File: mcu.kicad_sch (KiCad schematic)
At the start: 11 parts, among them U5 ESP32-S3-WROOM-1

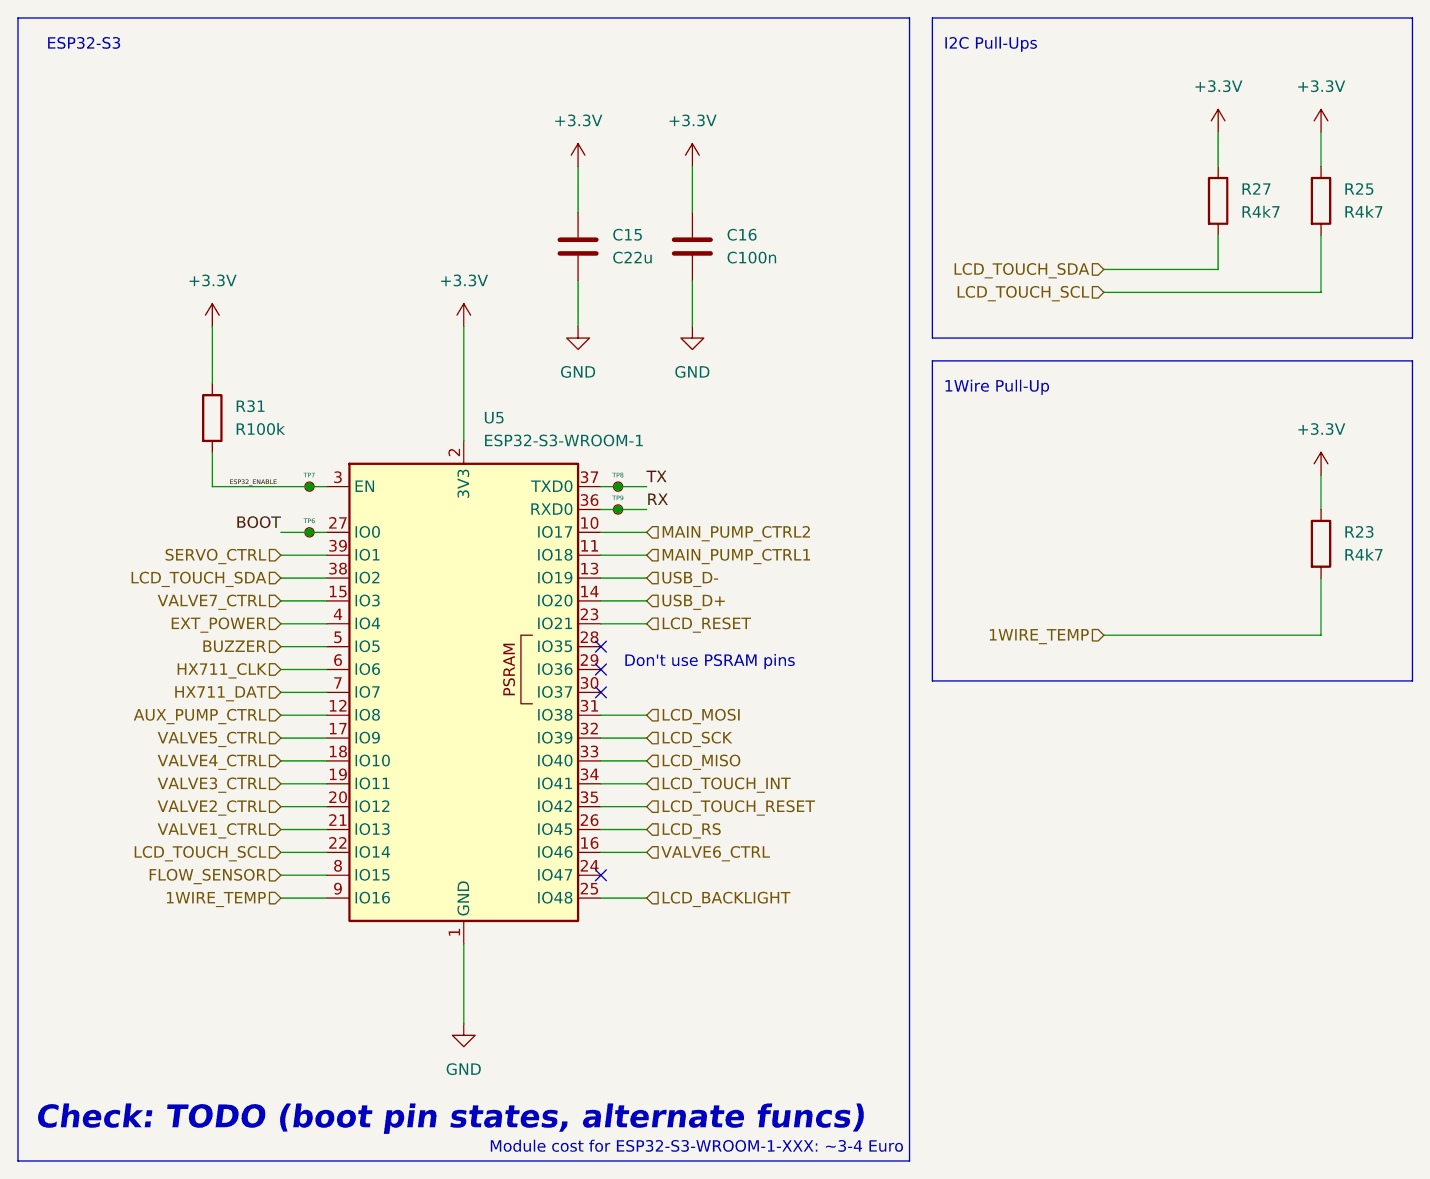
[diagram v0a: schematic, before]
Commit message: Reannotate geographically by layout
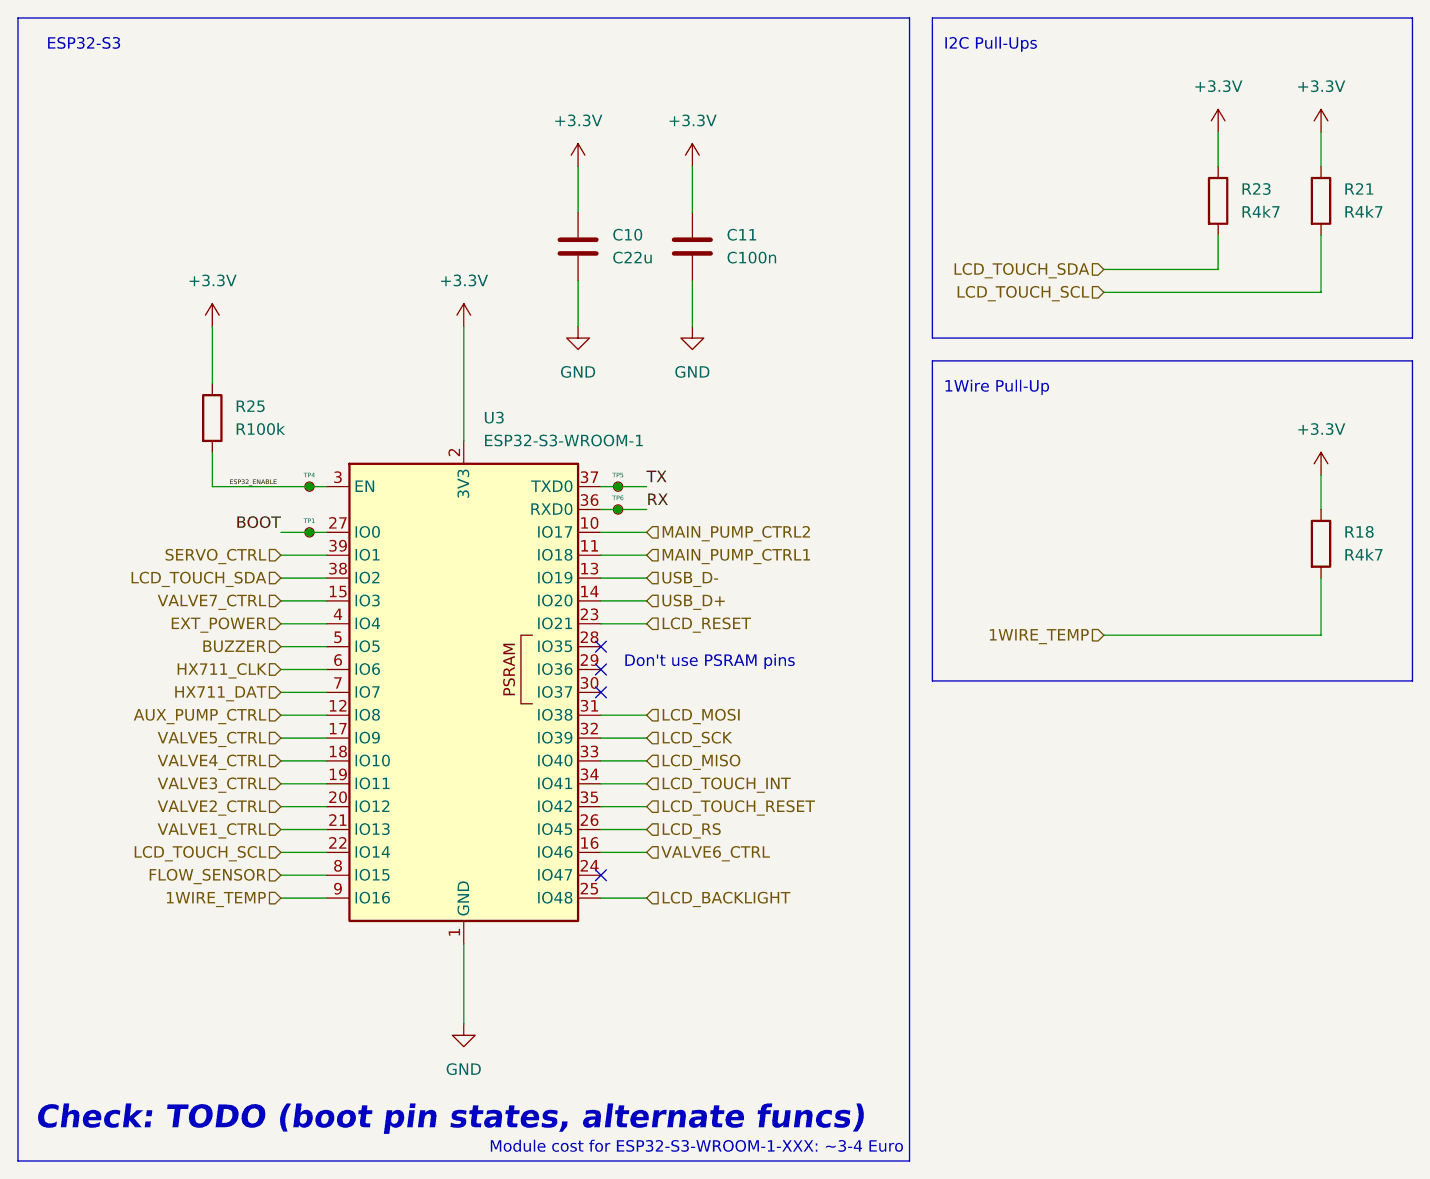
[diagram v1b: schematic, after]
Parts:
- renumbered C15 to C10, C16 to C11, R23 to R18, R25 to R21, R27 to R23, R31 to R25, TP6 to TP1, TP7 to TP4, TP8 to TP5, TP9 to TP6, U5 to U3
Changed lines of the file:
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@@
   (symbol (lib_id "Connector:TestPoint_Small") (at 46.355 82.55 0) (unit 1)
     (in_bom yes) (on_board yes) (dnp no)
-    (property "Reference" "TP7" (at 46.355 81.28 0)
+    (property "Reference" "TP4" (at 46.355 81.28 0)
       (effects (font (size 0.504 0.504)))
     )
@@
       (project "mainboard"
         (path "/613f8c39-c37c-4981-8911-5138d36a7959/ed2e236e-cfd2-4567-8f0f-a7cfa7de4717"
-          (reference "TP7") (unit 1)
+          (reference "TP4") (unit 1)
         )
       )
@@
   (symbol (lib_id "Connector:TestPoint_Small") (at 80.645 82.55 0) (unit 1)
     (in_bom yes) (on_board yes) (dnp no)
-    (property "Reference" "TP8" (at 80.645 81.28 0)
+    (property "Reference" "TP5" (at 80.645 81.28 0)
       (effects (font (size 0.504 0.504)))
     )
@@
       (project "mainboard"
         (path "/613f8c39-c37c-4981-8911-5138d36a7959/ed2e236e-cfd2-4567-8f0f-a7cfa7de4717"
-          (reference "TP8") (unit 1)
+          (reference "TP5") (unit 1)
         )
       )
@@
   (symbol (lib_id "Device:C") (at 76.2 55.88 0) (unit 1)
     (in_bom yes) (on_board yes) (dnp no) (fields_autoplaced)
-    (property "Reference" "C15" (at 80.01 54.61 0)
+    (property "Reference" "C10" (at 80.01 54.61 0)
       (effects (font (size 1.27 1.27)) (justify left))
     )
@@
       (project "mainboard"
         (path "/613f8c39-c37c-4981-8911-5138d36a7959/ed2e236e-cfd2-4567-8f0f-a7cfa7de4717"
-          (reference "C15") (unit 1)
+          (reference "C10") (unit 1)
         )
       )
@@
   (symbol (lib_id "Connector:TestPoint_Small") (at 80.645 85.09 0) (unit 1)
     (in_bom yes) (on_board yes) (dnp no)
-    (property "Reference" "TP9" (at 80.645 83.82 0)
+    (property "Reference" "TP6" (at 80.645 83.82 0)
       (effects (font (size 0.504 0.504)))
     )
@@
       (project "mainboard"
         (path "/613f8c39-c37c-4981-8911-5138d36a7959/ed2e236e-cfd2-4567-8f0f-a7cfa7de4717"
-          (reference "TP9") (unit 1)
+          (reference "TP6") (unit 1)
         )
       )
@@
   (symbol (lib_id "Device:R") (at 158.75 50.8 0) (unit 1)
     (in_bom yes) (on_board yes) (dnp no) (fields_autoplaced)
-    (property "Reference" "R25" (at 161.29 49.53 0)
+    (property "Reference" "R21" (at 161.29 49.53 0)
       (effects (font (size 1.27 1.27)) (justify left))
     )
@@
       (project "mainboard"
         (path "/613f8c39-c37c-4981-8911-5138d36a7959/ed2e236e-cfd2-4567-8f0f-a7cfa7de4717"
-          (reference "R25") (unit 1)
+          (reference "R21") (unit 1)
         )
       )
@@
   (symbol (lib_id "Connector:TestPoint_Small") (at 46.355 87.63 0) (unit 1)
     (in_bom yes) (on_board yes) (dnp no)
-    (property "Reference" "TP6" (at 46.355 86.36 0)
+    (property "Reference" "TP1" (at 46.355 86.36 0)
       (effects (font (size 0.504 0.504)))
     )
@@
       (project "mainboard"
         (path "/613f8c39-c37c-4981-8911-5138d36a7959/ed2e236e-cfd2-4567-8f0f-a7cfa7de4717"
-          (reference "TP6") (unit 1)
+          (reference "TP1") (unit 1)
         )
       )
@@
   (symbol (lib_id "RF_Module:ESP32-S3-WROOM-1") (at 63.5 105.41 0) (unit 1)
     (in_bom yes) (on_board yes) (dnp no) (fields_autoplaced)
-    (property "Reference" "U5" (at 65.6941 74.93 0)
+    (property "Reference" "U3" (at 65.6941 74.93 0)
       (effects (font (size 1.27 1.27)) (justify left))
     )
@@
       (project "mainboard"
         (path "/613f8c39-c37c-4981-8911-5138d36a7959/ed2e236e-cfd2-4567-8f0f-a7cfa7de4717"
-          (reference "U5") (unit 1)
+          (reference "U3") (unit 1)
         )
       )
@@
   (symbol (lib_id "Device:R") (at 147.32 50.8 0) (unit 1)
     (in_bom yes) (on_board yes) (dnp no) (fields_autoplaced)
-    (property "Reference" "R27" (at 149.86 49.53 0)
+    (property "Reference" "R23" (at 149.86 49.53 0)
       (effects (font (size 1.27 1.27)) (justify left))
     )
@@
       (project "mainboard"
         (path "/613f8c39-c37c-4981-8911-5138d36a7959/ed2e236e-cfd2-4567-8f0f-a7cfa7de4717"
-          (reference "R27") (unit 1)
+          (reference "R23") (unit 1)
         )
       )
@@
   (symbol (lib_id "Device:R") (at 35.56 74.93 0) (unit 1)
     (in_bom yes) (on_board yes) (dnp no) (fields_autoplaced)
-    (property "Reference" "R31" (at 38.1 73.66 0)
+    (property "Reference" "R25" (at 38.1 73.66 0)
       (effects (font (size 1.27 1.27)) (justify left))
     )
@@
       (project "mainboard"
         (path "/613f8c39-c37c-4981-8911-5138d36a7959/ed2e236e-cfd2-4567-8f0f-a7cfa7de4717"
-          (reference "R31") (unit 1)
+          (reference "R25") (unit 1)
         )
       )
@@
   (symbol (lib_id "Device:R") (at 158.75 88.9 0) (unit 1)
     (in_bom yes) (on_board yes) (dnp no) (fields_autoplaced)
-    (property "Reference" "R23" (at 161.29 87.63 0)
+    (property "Reference" "R18" (at 161.29 87.63 0)
       (effects (font (size 1.27 1.27)) (justify left))
     )
@@
       (project "mainboard"
         (path "/613f8c39-c37c-4981-8911-5138d36a7959/ed2e236e-cfd2-4567-8f0f-a7cfa7de4717"
-          (reference "R23") (unit 1)
+          (reference "R18") (unit 1)
         )
       )
@@
   (symbol (lib_id "Device:C") (at 88.9 55.88 0) (unit 1)
     (in_bom yes) (on_board yes) (dnp no) (fields_autoplaced)
-    (property "Reference" "C16" (at 92.71 54.61 0)
+    (property "Reference" "C11" (at 92.71 54.61 0)
       (effects (font (size 1.27 1.27)) (justify left))
     )
@@
       (project "mainboard"
         (path "/613f8c39-c37c-4981-8911-5138d36a7959/ed2e236e-cfd2-4567-8f0f-a7cfa7de4717"
-          (reference "C16") (unit 1)
-        )
-      )
+          (reference "C11") (unit 1)
+        )
+      )

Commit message: Fix revision
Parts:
- U3: value ESP32-S3-WROOM-1 -> ESP32-S3-WROOM-1-N4R2; Mouser Part Number 356-ESP32-S3WROOM1N4 -> 356-ESP32S3WROM1N4R2
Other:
- title: openautolab - Mainboard -> openautolab - Alternative Mainboard
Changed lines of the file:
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@@
   (paper "A4")
   (title_block
-    (title "openautolab - Mainboard")
+    (title "openautolab - Alternative Mainboard")
     (date "2024-04-03")
-    (rev "2.0")
+    (rev "1")
   )
   (junction (at 80.645 82.55) (diameter 0) (color 0 0 0 0)
@@
       (effects (font (size 1.27 1.27)) (justify left))
     )
-    (property "Value" "ESP32-S3-WROOM-1" (at 65.6941 77.47 0)
+    (property "Value" "ESP32-S3-WROOM-1-N4R2" (at 65.6941 77.47 0)
       (effects (font (size 1.27 1.27)) (justify left))
     )
@@
       (effects (font (size 1.27 1.27)) hide)
     )
-    (property "Mouser Part Number" "356-ESP32-S3WROOM1N4" (at 63.5 105.41 0)
-      (effects (font (size 1.27 1.27)) hide)
-    )
+    (property "Mouser Part Number" "356-ESP32S3WROM1N4R2" (at 63.5 105.41 0)
+      (effects (font (size 1.27 1.27)) hide)
+    )
